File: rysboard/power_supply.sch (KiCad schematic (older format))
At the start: 36 parts, among them J19 Fan_Connector, Q1 DMP3036SSD-13, Q3 NST847BDP6T5G, Q5 DMP3036SSD-13, U3 ST1S10, U6 L78L33_SO8

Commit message: started board project
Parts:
- gave numbers to parts that had none: 5
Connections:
- net +12V: now also Q1.5 (d), Q1.6 (d); no longer Q1.7 (d), Q1.8 (d)
- net +BATT: now also Q1.3 (S2); no longer Q1.1 (S1)
- net at C16.1, C17.1, C18.1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: now also Q1.7 (d), Q1.8 (d); no longer Q5.7 (d), Q5.8 (d)
- net at D14.2 (A), Q3.3 (C2), R12.2: now also Q1.2 (G1); no longer Q5.2 (G1)
- net at D13.2 (A), Q3.6 (C1), R7.2: now also Q5.2 (G1); no longer Q1.2 (G1)
- net at R8.2: now also Q4.2 (B1); no longer Q4.5 (B2)
- new net: J19.2 (Pin_2), Q5.7 (d), Q5.8 (d)
- new net: Q1.4 (G2), Q4.6 (C1), R10.2
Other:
- moved on the sheet: Q1A, Q5A
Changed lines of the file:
@@
 L rysboard:DMP3036SSD-13 Q5
 U 1 1 6051EA37
+P 2275 4025
+F 0 "Q5" V 2617 4025 50  0000 C CNN
+F 1 "DMP3036SSD-13" V 2526 4025 50  0000 C CNN
+F 2 "Package_SO:SO-8_3.9x4.9mm_P1.27mm" H 2475 3950 50  0001 L CIN
+F 3 "" H 2275 4025 50  0001 L CNN
+	1    2275 4025
+	0    1    -1   0
+$EndComp
+$Comp
+L rysboard:DMP3036SSD-13 Q1
+U 1 1 605FF267
 P 6000 1450
-F 0 "Q5" V 6342 1450 50  0000 C CNN
+F 0 "Q1" V 6342 1450 50  0000 C CNN
 F 1 "DMP3036SSD-13" V 6251 1450 50  0000 C CNN
 F 2 "Package_SO:SO-8_3.9x4.9mm_P1.27mm" H 6200 1375 50  0001 L CIN
 F 3 "" H 6000 1450 50  0001 L CNN
 	1    6000 1450
-	0    1    -1   0
-$EndComp
-$Comp
-L rysboard:DMP3036SSD-13 Q1
-U 1 1 605FF267
-P 2275 4025
-F 0 "Q1" V 2617 4025 50  0000 C CNN
-F 1 "DMP3036SSD-13" V 2526 4025 50  0000 C CNN
-F 2 "Package_SO:SO-8_3.9x4.9mm_P1.27mm" H 2475 3950 50  0001 L CIN
-F 3 "" H 2275 4025 50  0001 L CNN
-	1    2275 4025
 	0    1    -1   0
 $EndComp
@@
 	2175 1825 1675 1825
 $Comp
-L rysboard:DMP3036SSD-13 Q?
-U 1 1 60615F71
+L rysboard:DMP3036SSD-13 Q1
+U 2 1 60615F71
 P 3650 1275
-F 0 "Q?" V 3992 1275 50  0000 C CNN
+F 0 "Q1" V 3992 1275 50  0000 C CNN
 F 1 "DMP3036SSD-13" V 3901 1275 50  0000 C CNN
 F 2 "Package_SO:SO-8_3.9x4.9mm_P1.27mm" H 3850 1200 50  0001 L CIN
 F 3 "" H 3650 1275 50  0001 L CNN
-	1    3650 1275
+	2    3650 1275
 	0    1    -1   0
 $EndComp
 $Comp
-L Device:D_Zener D?
+L Device:D_Zener D3
 U 1 1 60616F79
 P 2925 1325
-F 0 "D?" V 2850 950 50  0000 L CNN
+F 0 "D3" V 2850 950 50  0000 L CNN
 F 1 "TSZU52C10 RG" V 3000 700 50  0000 L CNN
 F 2 "Diode_SMD:D_0603_1608Metric" H 2925 1325 50  0001 C CNN
@@
 $EndComp
 $Comp
-L Device:R R?
+L Device:R R10
 U 1 1 606173BC
 P 3225 1325
-F 0 "R?" H 3295 1371 50  0000 L CNN
+F 0 "R10" H 3295 1371 50  0000 L CNN
 F 1 "110KR" H 3295 1280 50  0000 L CNN
 F 2 "Resistor_SMD:R_0603_1608Metric" V 3155 1325 50  0001 C CNN
@@
 $EndComp
 $Comp
-L rysboard:NST847BDP6T5G Q?
-U 2 1 6061762B
+L rysboard:NST847BDP6T5G Q4
+U 1 1 6061762B
 P 3550 1875
-F 0 "Q?" H 3740 1921 50  0000 L CNN
+F 0 "Q4" H 3740 1921 50  0000 L CNN
 F 1 "NST847BDP6T5G" H 3740 1830 50  0000 L CNN
 F 2 "Package_TO_SOT_SMD:SOT-963" H 3750 1975 50  0001 C CNN
 F 3 "~" H 3550 1875 50  0001 C CNN
-	2    3550 1875
-	1    0    0    -1
-$EndComp
-$Comp
-L Device:R R?
+	1    3550 1875
+	1    0    0    -1
+$EndComp
+$Comp
+L Device:R R8
 U 1 1 60617A11
 P 3200 1875
-F 0 "R?" V 3280 1875 50  0000 C CNN
+F 0 "R8" V 3280 1875 50  0000 C CNN
 F 1 "10k" V 3200 1875 50  0000 C CNN
 F 2 "Resistor_SMD:R_0603_1608Metric" V 3130 1875 50  0001 C CNN
@@
 $EndComp
 $Comp
-L power:+BATT #PWR?
+L power:+BATT #PWR020
 U 1 1 60617D1F
 P 2925 1175
-F 0 "#PWR?" H 2925 1025 50  0001 C CNN
+F 0 "#PWR020" H 2925 1025 50  0001 C CNN
 F 1 "+BATT" H 2940 1348 50  0000 C CNN
 F 2 "" H 2925 1175 50  0001 C CNN
@@
 Connection ~ 3650 1475
 $Comp
-L power:GND #PWR?
+L power:GND #PWR024
 U 1 1 606277F2
 P 3625 2050
-F 0 "#PWR?" H 3625 1800 50  0001 C CNN
+F 0 "#PWR024" H 3625 1800 50  0001 C CNN
 F 1 "GND" H 3630 1877 50  0000 C CNN
 F 2 "" H 3625 2050 50  0001 C CNN
@@
 $EndComp
 $Comp
-L power:+12V #PWR?
+L power:+12V #PWR035
 U 1 1 60627A51
 P 4125 1175
-F 0 "#PWR?" H 4125 1025 50  0001 C CNN
+F 0 "#PWR035" H 4125 1025 50  0001 C CNN
 F 1 "+12V" H 4140 1348 50  0000 C CNN
 F 2 "" H 4125 1175 50  0001 C CNN
@@
 Wire Wire Line
 	4125 1175 3850 1175
+Connection ~ 6000 1650
 $EndSCHEMATC

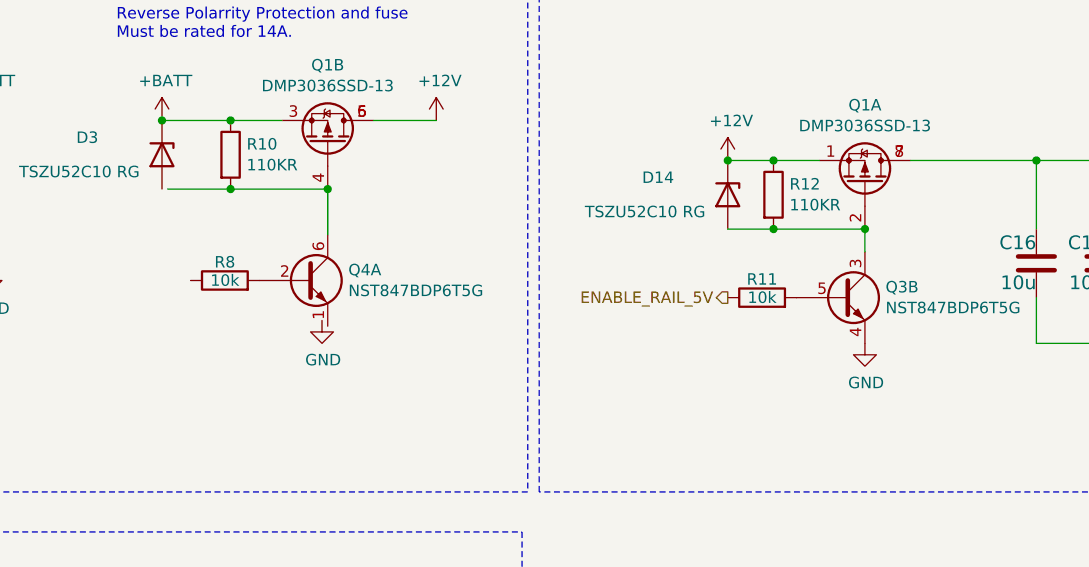
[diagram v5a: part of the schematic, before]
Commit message: fixed some bugs. Input protection done. Started implementing 5V Regulator
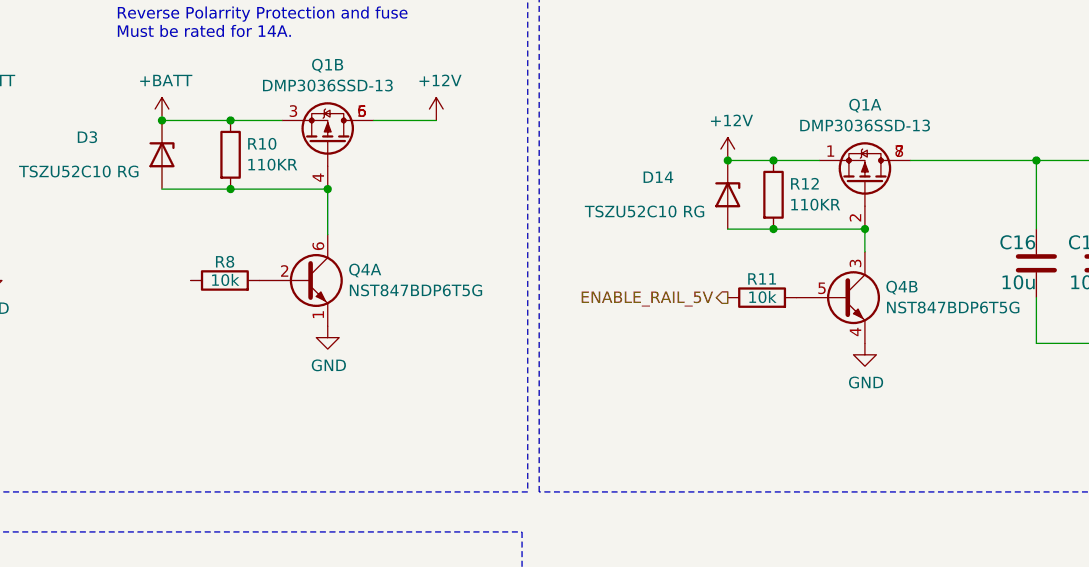
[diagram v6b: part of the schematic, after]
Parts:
- renumbered Q3 to Q4
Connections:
- net GND: now also Q4.1 (E1)
- net at Q1.4 (G2), Q4.6 (C1), R10.2: now also D3.2 (A)
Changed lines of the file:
@@
 PWM_FAN
 $Comp
-L rysboard:NST847BDP6T5G Q3
+L rysboard:NST847BDP6T5G Q4
 U 2 1 606E7E9A
 P 5900 1950
-F 0 "Q3" H 6090 1996 50  0000 L CNN
+F 0 "Q4" H 6090 1996 50  0000 L CNN
 F 1 "NST847BDP6T5G" H 6090 1905 50  0000 L CNN
 F 2 "Package_TO_SOT_SMD:SOT-963" H 6100 2050 50  0001 C CNN
@@
 Wire Wire Line
 	3225 1475 3650 1475
-Wire Wire Line
-	2950 1475 3225 1475
 Connection ~ 3225 1475
 Wire Wire Line
@@
 L power:GND #PWR024
 U 1 1 606277F2
-P 3625 2050
-F 0 "#PWR024" H 3625 1800 50  0001 C CNN
-F 1 "GND" H 3630 1877 50  0000 C CNN
-F 2 "" H 3625 2050 50  0001 C CNN
-F 3 "" H 3625 2050 50  0001 C CNN
-	1    3625 2050
+P 3650 2075
+F 0 "#PWR024" H 3650 1825 50  0001 C CNN
+F 1 "GND" H 3655 1902 50  0000 C CNN
+F 2 "" H 3650 2075 50  0001 C CNN
+F 3 "" H 3650 2075 50  0001 C CNN
+	1    3650 2075
 	1    0    0    -1
 $EndComp
@@
 	4125 1175 3850 1175
 Connection ~ 6000 1650
+Wire Wire Line
+	2925 1475 3225 1475
 $EndSCHEMATC

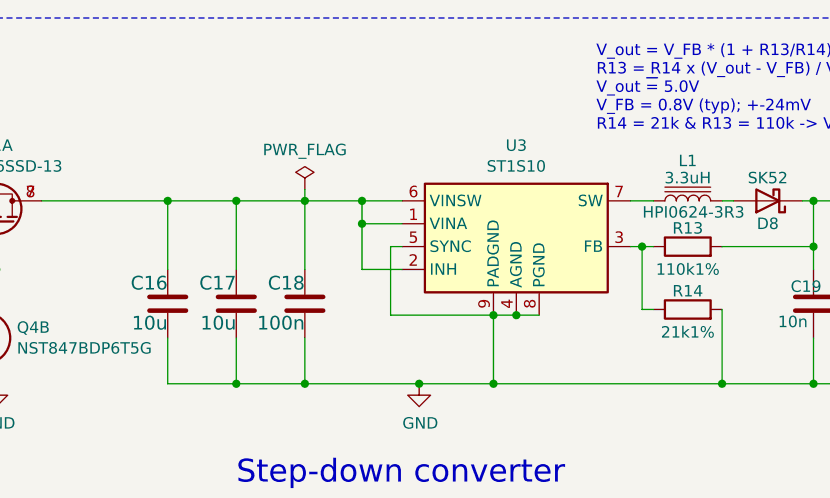
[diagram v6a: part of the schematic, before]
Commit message: st motor drivers done
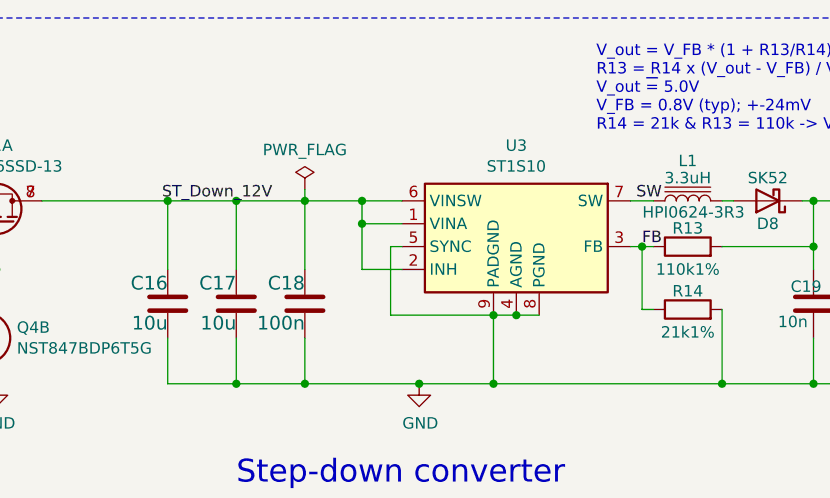
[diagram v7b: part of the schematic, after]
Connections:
- net ST_Down_12V: now reaches C16.1, C17.1, C18.1, Q1.7 (d), Q1.8 (d), U3.1 (VINA), U3.2 (INH), U3.6 (VINSW)
- net FB: now reaches R13.1, R14.1, U3.3 (FB)
- net SW: now reaches L1.1, U3.7 (SW)
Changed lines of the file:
@@
 Wire Wire Line
 	2925 1475 3225 1475
+Text Label 8800 1350 0    50   ~ 0
+SW
+Text Label 8825 1550 0    50   ~ 0
+FB
+Text Label 6725 1350 0    50   ~ 0
+ST_Down_12V
 $EndSCHEMATC

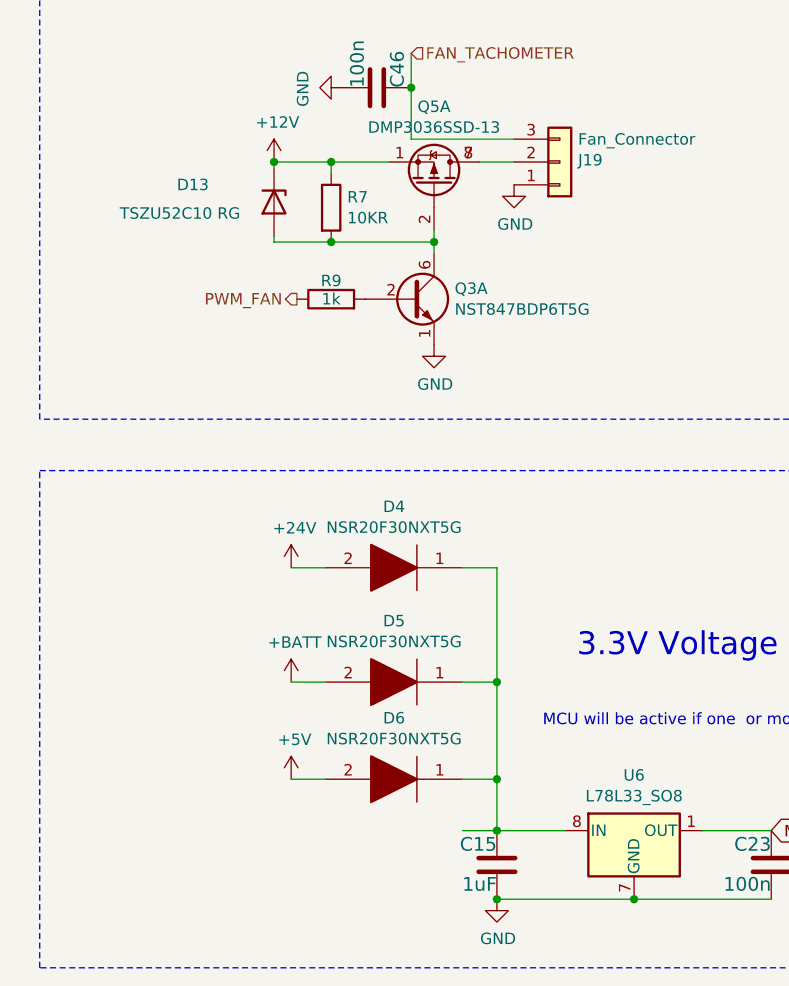
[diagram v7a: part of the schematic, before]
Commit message: 3,3Vreg added. MCU first placement
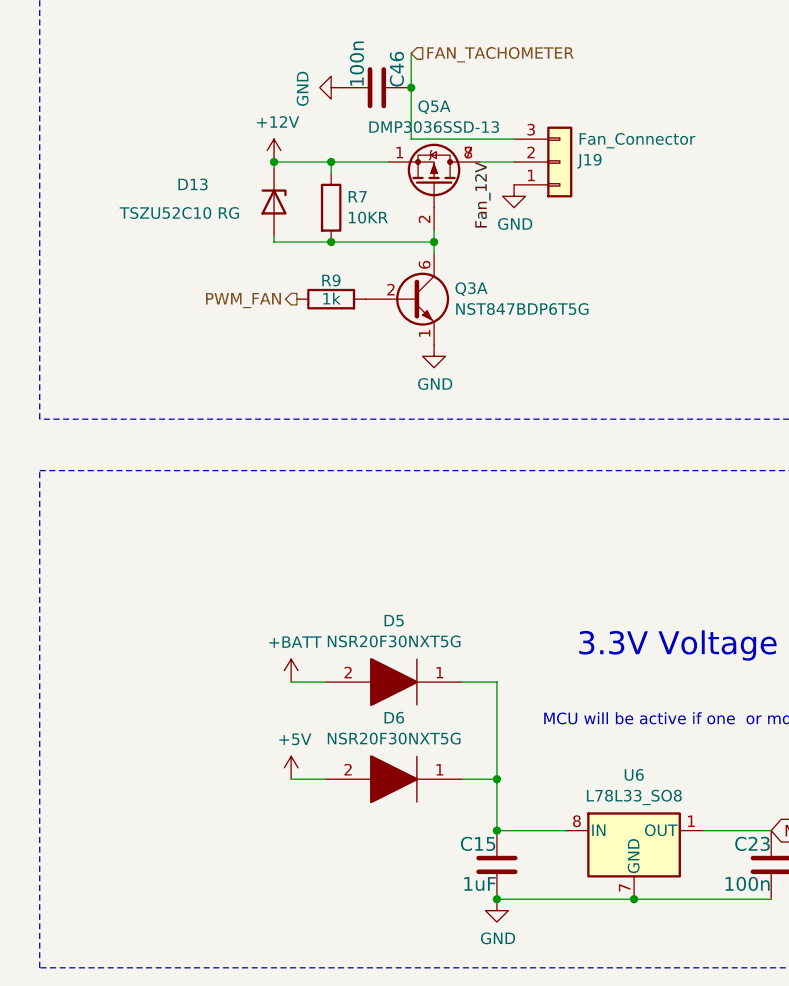
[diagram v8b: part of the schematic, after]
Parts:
- removed D4: NSR20F30NXT5G, SamacSys_Parts:DSN2_1, symbol SamacSys_Parts:NSR20F30NXT5G
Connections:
- net Fan_12V: now reaches J19.2 (Pin_2), Q5.7 (d), Q5.8 (d)
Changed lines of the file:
@@
 	1    0    0    -1
 $EndComp
-Wire Wire Line
-	2400 6850 2550 6850
 Connection ~ 2550 6850
 Text Notes 2725 825  0    50   ~ 0
@@
 	1650 6200 1800 6200
 $Comp
-L power:+24V #PWR025
-U 1 1 606699BF
-P 1650 5700
-F 0 "#PWR025" H 1650 5550 50  0001 C CNN
-F 1 "+24V" H 1665 5873 50  0000 C CNN
-F 2 "" H 1650 5700 50  0001 C CNN
-F 3 "" H 1650 5700 50  0001 C CNN
-	1    1650 5700
-	1    0    0    -1
-$EndComp
-Wire Wire Line
-	1650 5700 1800 5700
-Wire Wire Line
-	2550 5700 2400 5700
-$Comp
 L power:+5V #PWR029
 U 1 1 6067B267
@@
 	0    1    -1   0
 $EndComp
-$Comp
-L SamacSys_Parts:NSR20F30NXT5G D4
-U 1 1 60433DC9
-P 2400 5700
-F 0 "D4" H 2700 5433 50  0000 C CNN
-F 1 "NSR20F30NXT5G" H 2700 5524 50  0000 C CNN
-F 2 "SamacSys_Parts:DSN2_1" H 2850 5700 50  0001 L CNN
-F 3 "http://www.onsemi.com/pub/Collateral/NSR20F30-D.PDF" H 2850 5600 50  0001 L CNN
-F 4 "ON SEMICONDUCTOR - NSR20F30NXT5G - DIODE, SCHOTTKY, 2A, 30V, 0603" H 2850 5500 50  0001 L CNN "Description"
-F 5 "" H 2850 5400 50  0001 L CNN "Height"
-F 6 "863-NSR20F30NXT5G" H 2850 5300 50  0001 L CNN "Mouser Part Number"
-F 7 "https://www.mouser.co.uk/ProductDetail/ON-Semiconductor/NSR20F30NXT5G/?qs=3ezCrKCRT5K%2FARb%252BJ8n8Hg%3D%3D" H 2850 5200 50  0001 L CNN "Mouser Price/Stock"
-F 8 "ON Semiconductor" H 2850 5100 50  0001 L CNN "Manufacturer_Name"
-F 9 "NSR20F30NXT5G" H 2850 5000 50  0001 L CNN "Manufacturer_Part_Number"
-	1    2400 5700
-	-1   0    0    1
-$EndComp
-Wire Wire Line
-	2550 5700 2550 6200
 $Comp
 L SamacSys_Parts:NSR20F30NXT5G D5
@@
 Wire Wire Line
 	2400 6200 2550 6200
-Connection ~ 2550 6200
 Wire Wire Line
 	2550 6200 2550 6625
@@
 Text Label 6725 1350 0    50   ~ 0
 ST_Down_12V
+Text Label 2525 3925 3    50   ~ 0
+Fan_12V
 $EndSCHEMATC
